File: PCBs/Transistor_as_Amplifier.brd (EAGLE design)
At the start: 37.5 x 25.9 mm, 12 parts, among them T1 BC547N

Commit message: New Update
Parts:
- moved R2 1.12 mm to (7.94, 18.7)
- moved R4 1.12 mm to (8.49, 21.8)
- moved T1 1.12 mm to (4.08, 13.5)
- moved R3 1.00 mm to (23.6, 21.8)
- moved C1 0.50 mm to (25.7, 13.8)
- moved C3 0.50 mm to (19.4, 14.2)
- moved R1 0.47 mm to (23.6, 18.5)
- moved INPUT 0.20 mm to (4.69, 7.14)
- moved GND 0.16 mm to (27.3, 7.00)
- moved 12V 0.10 mm to (19.8, 7.09)
- moved OUTPUT 0.08 mm to (12.3, 7.10)
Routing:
- net N$3: track 57.6 -> 0.00 mm
- net 12V: track 32.6 -> 0.00 mm
- net N$2: track 30.7 -> 0.00 mm
- net GND: track 29.8 -> 0.00 mm
- net N$1: track 26.4 -> 0.00 mm
- net N$4: track 16.3 -> 0.00 mm
- net N$7: track 9.95 -> 0.00 mm
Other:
- board size 37.5 x 25.9 mm -> 37 x 25.9 mm

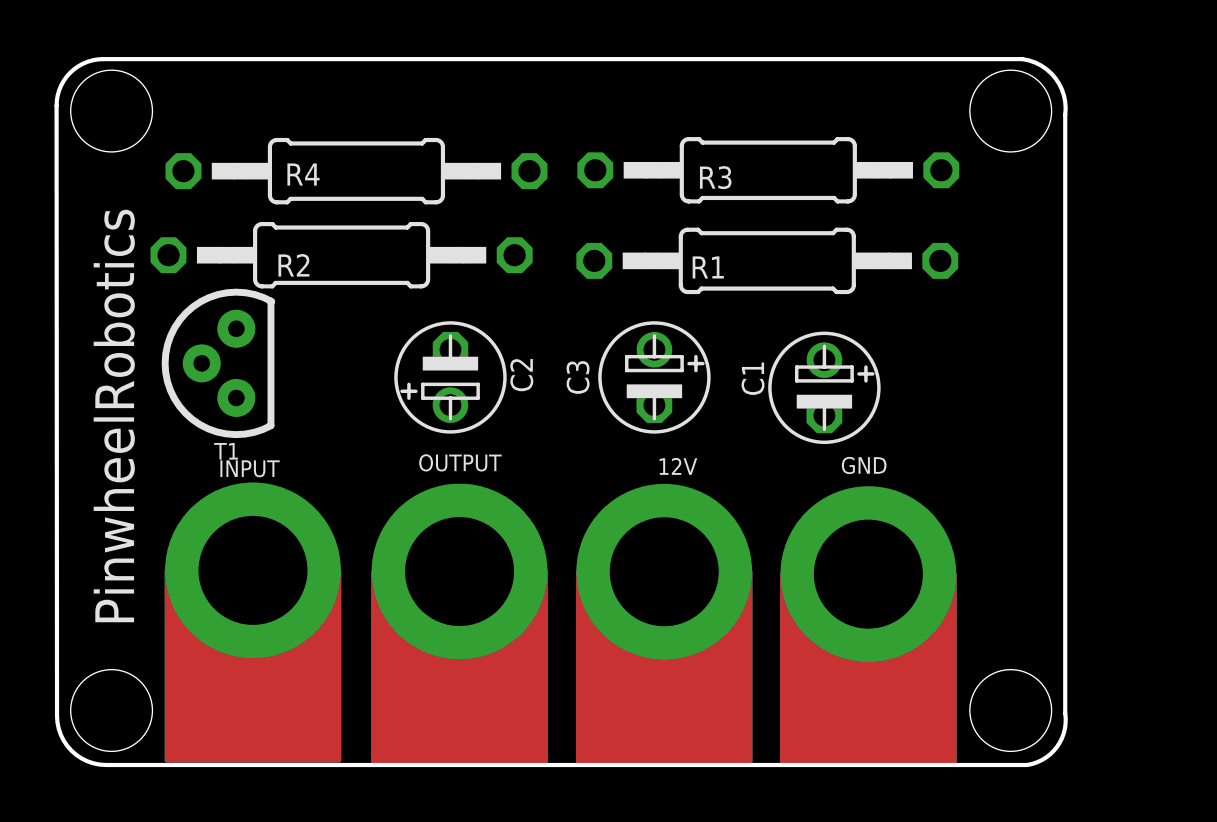
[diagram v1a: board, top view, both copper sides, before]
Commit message: New Update for board curv
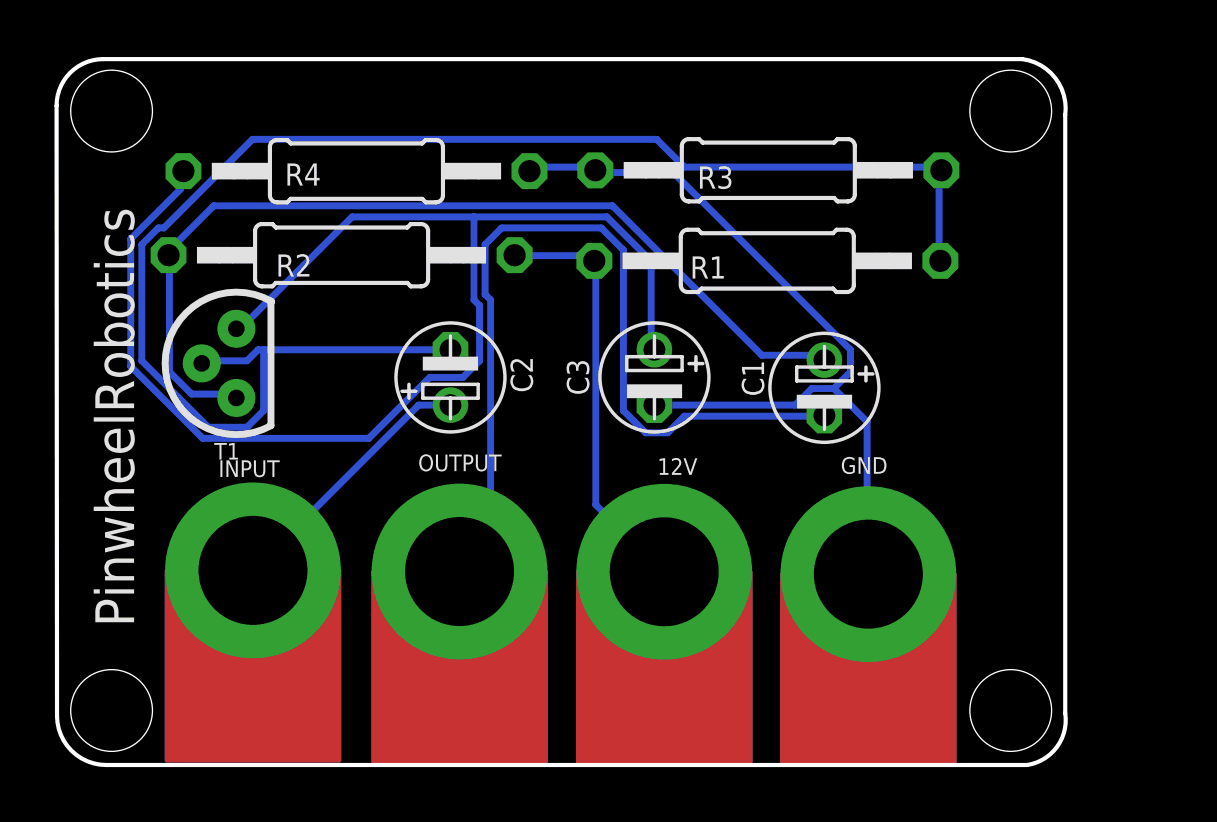
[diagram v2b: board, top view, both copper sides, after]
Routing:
- net N$3: track 0.00 -> 56.4 mm
- net N$1: track 0.00 -> 49.4 mm
- net N$2: track 0.00 -> 34.5 mm
- net N$4: track 0.00 -> 32.1 mm
- net GND: track 0.00 -> 30.5 mm
- net 12V: track 0.00 -> 15.5 mm
- net N$7: track 0.00 -> 9.76 mm

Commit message: Dimension added
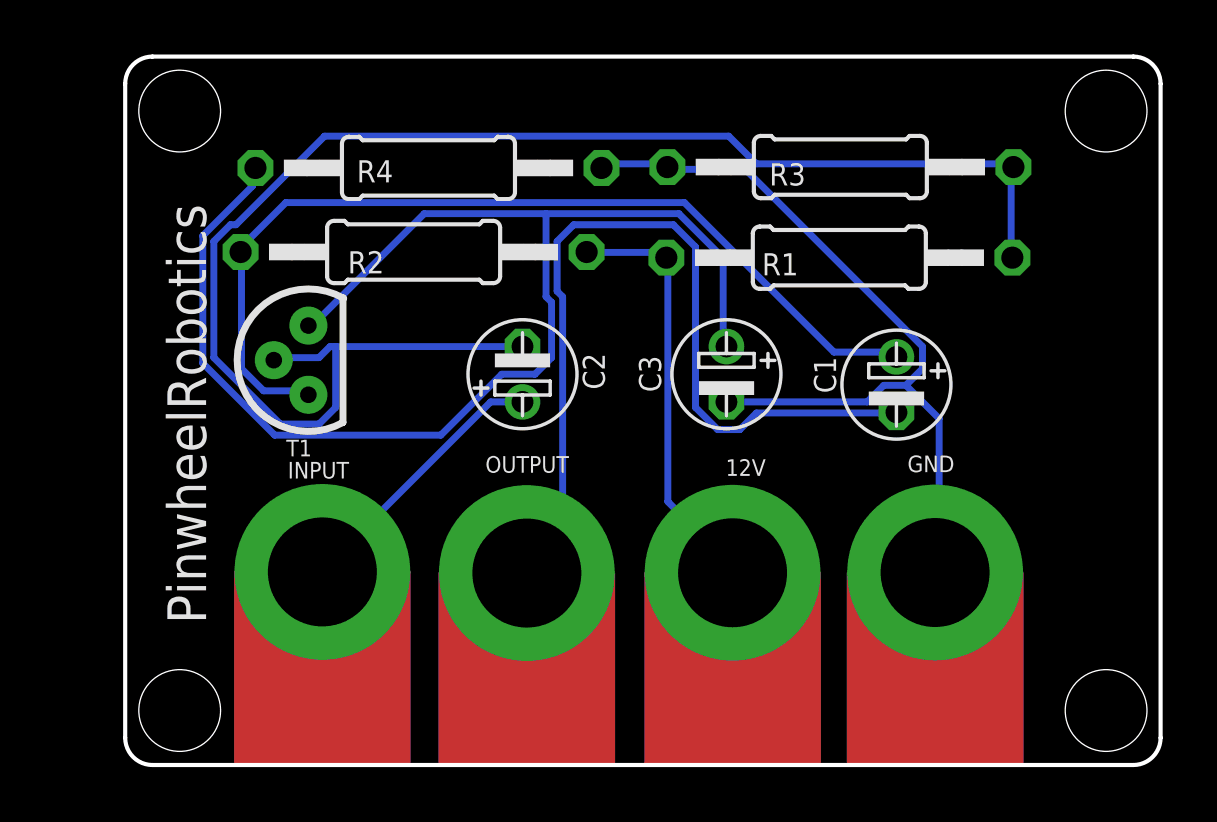
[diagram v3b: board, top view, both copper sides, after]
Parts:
- moved C3 2.65 mm to (22.1, 14.3)
- moved C1 2.65 mm to (28.3, 14.0)
- moved C2 2.65 mm to (14.6, 14.3)
- moved R1 2.65 mm to (26.2, 18.6)
- moved R2 2.65 mm to (10.6, 18.8)
- moved R3 2.65 mm to (26.2, 21.9)
- moved R4 2.65 mm to (11.1, 21.9)
- moved T1 2.65 mm to (6.72, 13.6)
- moved INPUT 2.55 mm to (7.24, 7.09)
- moved 12V 2.51 mm to (22.3, 7.06)
- moved OUTPUT 2.47 mm to (14.7, 7.04)
- moved GND 2.45 mm to (29.7, 7.06)
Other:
- board size 37 x 25.9 mm -> 38 x 26 mm
